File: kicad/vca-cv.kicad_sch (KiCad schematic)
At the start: 9 parts, among them Q14 2N3906, U19 TL072

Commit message: component positioning mostly done
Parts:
- C57, C58, C59: footprint rumblesan-standard-parts:C_Rect_L7.0mm_W3.5mm_P5.00mm -> rumblesan-standard-parts:C_Rect_L7.0mm_W2.5mm_P5.00mm
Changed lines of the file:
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@@
     (property "Reference" "C57" (id 0) (at 133.35 77.9612 90))
     (property "Value" "220pF" (id 1) (at 133.35 80.4981 90))
-    (property "Footprint" "rumblesan-standard-parts:C_Rect_L7.0mm_W3.5mm_P5.00mm" (id 2) (at 132.08 78.105 0)
+    (property "Footprint" "rumblesan-standard-parts:C_Rect_L7.0mm_W2.5mm_P5.00mm" (id 2) (at 132.08 78.105 0)
       (effects (font (size 1.27 1.27)) hide)
     )
@@
       (effects (font (size 1.27 1.27)) (justify left))
     )
-    (property "Footprint" "rumblesan-standard-parts:C_Rect_L7.0mm_W3.5mm_P5.00mm" (id 2) (at 215.265 60.96 90)
+    (property "Footprint" "rumblesan-standard-parts:C_Rect_L7.0mm_W2.5mm_P5.00mm" (id 2) (at 215.265 60.96 90)
       (effects (font (size 1.27 1.27)) hide)
     )
@@
       (effects (font (size 1.27 1.27)) (justify left))
     )
-    (property "Footprint" "rumblesan-standard-parts:C_Rect_L7.0mm_W3.5mm_P5.00mm" (id 2) (at 215.265 73.66 90)
-      (effects (font (size 1.27 1.27)) hide)
-    )
+    (property "Footprint" "rumblesan-standard-parts:C_Rect_L7.0mm_W2.5mm_P5.00mm" (id 2) (at 215.265 73.66 90)
+      (effects (font (size 1.27 1.27)) hide)
+    )

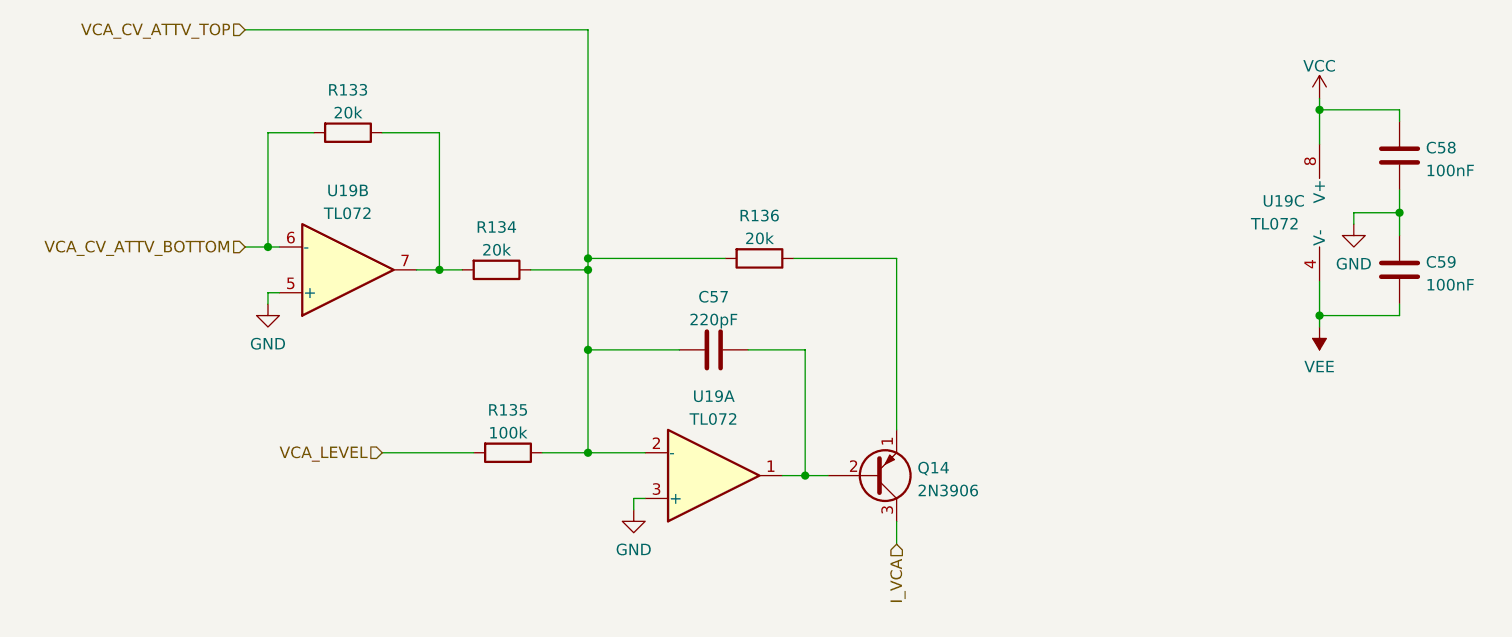
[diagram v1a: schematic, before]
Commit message: Full rejig to use attiny for divider
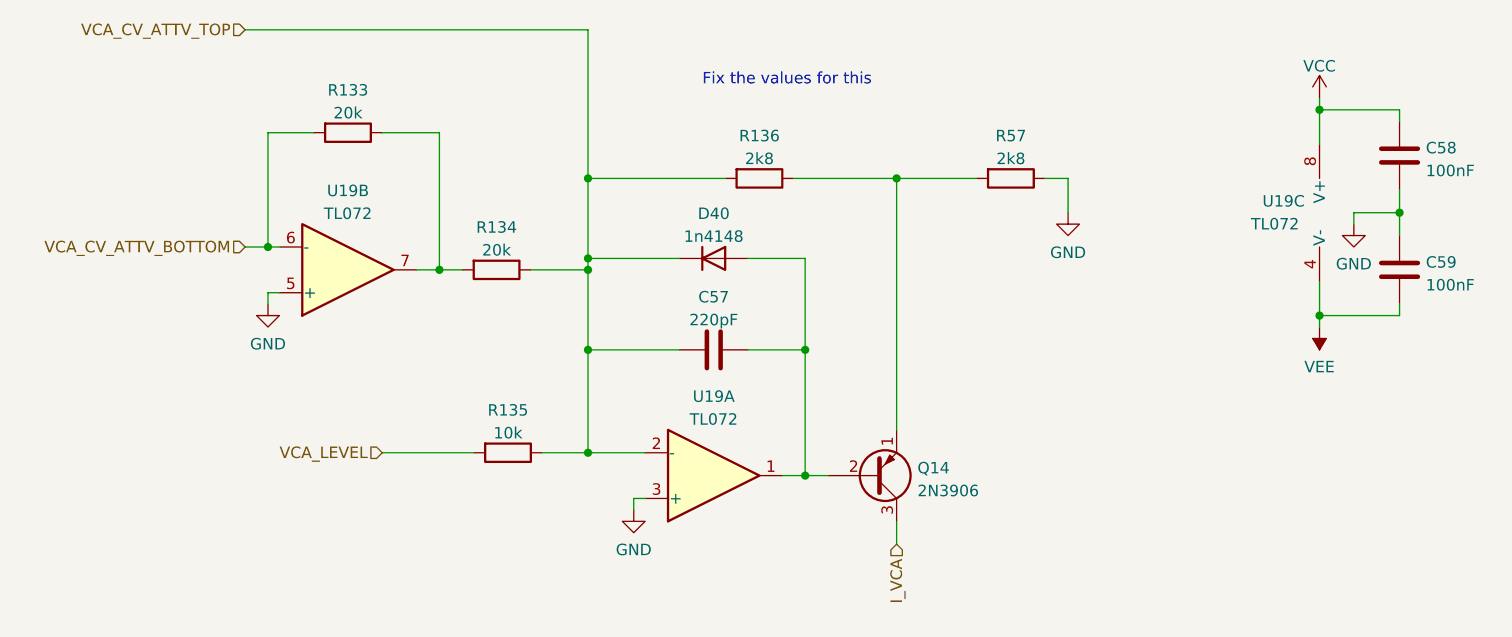
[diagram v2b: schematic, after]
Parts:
- added D40: 1n4148, rumblesan-standard-parts:D_DO-35_SOD27_P7.62mm_Horizontal, symbol Device:D
- added R57: 2k8, rumblesan-standard-parts:R_Axial_DIN0207_L6.3mm_D2.5mm_P10.16mm_Horizontal, symbol rumblesan-standard-parts:R
- C58, C59: Spec ceramic C0G -> ceramic X7R
- R135: value 100k -> 10k
- R136: value 20k -> 2k8
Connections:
- net GND: now also R57.1
- net VCA_CV_ATTV_TOP: now also D40.1 (K)
- net at C57.2, Q14.2 (B), U19.1: now also D40.2 (A)
- net at Q14.1 (E), R136.1: now also R57.2
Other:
- note added: "Fix the values for this"
- moved on the sheet: R136
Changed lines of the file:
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@@
     (comment 4 "Author: Guy John")
   )
+  (junction (at 143.51 83.82) (diameter 0) (color 0 0 0 0)
+  )
+  (junction (at 143.51 97.79) (diameter 0) (color 0 0 0 0)
+  )
+  (junction (at 102.87 74.93) (diameter 0) (color 0 0 0 0)
+  )
+  (junction (at 200.66 80.01) (diameter 0) (color 0 0 0 0)
+  )
+  (junction (at 119.38 74.93) (diameter 0) (color 0 0 0 0)
+  )
+  (junction (at 153.67 64.77) (diameter 0) (color 0 0 0 0)
+  )
+  (junction (at 209.55 68.58) (diameter 0) (color 0 0 0 0)
+  )
   (junction (at 119.38 73.66) (diameter 0) (color 0 0 0 0)
   )
-  (junction (at 143.51 97.79) (diameter 0) (color 0 0 0 0)
-  )
-  (junction (at 102.87 74.93) (diameter 0) (color 0 0 0 0)
-  )
-  (junction (at 200.66 80.01) (diameter 0) (color 0 0 0 0)
-  )
-  (junction (at 119.38 74.93) (diameter 0) (color 0 0 0 0)
-  )
-  (junction (at 209.55 68.58) (diameter 0) (color 0 0 0 0)
+  (junction (at 119.38 64.77) (diameter 0) (color 0 0 0 0)
   )
   (junction (at 83.82 72.39) (diameter 0) (color 0 0 0 0)
@@
   (junction (at 200.66 57.15) (diameter 0) (color 0 0 0 0)
   )
-  (wire (pts (xy 119.38 74.93) (xy 119.38 73.66))
-    (stroke (width 0) (type default) (color 0 0 0 0))
-  )
   (wire (pts (xy 153.67 102.87) (xy 153.67 105.41))
     (stroke (width 0) (type default) (color 0 0 0 0))
   )
+  (wire (pts (xy 170.18 64.77) (xy 172.72 64.77))
+    (stroke (width 0) (type default) (color 0 0 0 0))
+  )
   (wire (pts (xy 102.87 74.93) (xy 105.41 74.93))
     (stroke (width 0) (type default) (color 0 0 0 0))
@@
     (stroke (width 0) (type default) (color 0 0 0 0))
   )
-  (wire (pts (xy 153.67 73.66) (xy 153.67 92.71))
+  (wire (pts (xy 153.67 64.77) (xy 153.67 92.71))
+    (stroke (width 0) (type default) (color 0 0 0 0))
+  )
+  (wire (pts (xy 119.38 64.77) (xy 119.38 73.66))
+    (stroke (width 0) (type default) (color 0 0 0 0))
+  )
+  (wire (pts (xy 119.38 73.66) (xy 119.38 74.93))
     (stroke (width 0) (type default) (color 0 0 0 0))
   )
@@
     (stroke (width 0) (type default) (color 0 0 0 0))
   )
-  (wire (pts (xy 119.38 73.66) (xy 134.62 73.66))
+  (wire (pts (xy 119.38 64.77) (xy 134.62 64.77))
     (stroke (width 0) (type default) (color 0 0 0 0))
   )
@@
     (stroke (width 0) (type default) (color 0 0 0 0))
   )
-  (wire (pts (xy 142.24 73.66) (xy 153.67 73.66))
+  (wire (pts (xy 142.24 64.77) (xy 153.67 64.77))
     (stroke (width 0) (type default) (color 0 0 0 0))
   )
@@
     (stroke (width 0) (type default) (color 0 0 0 0))
   )
-  (wire (pts (xy 119.38 48.26) (xy 119.38 73.66))
+  (wire (pts (xy 153.67 64.77) (xy 162.56 64.77))
+    (stroke (width 0) (type default) (color 0 0 0 0))
+  )
+  (wire (pts (xy 119.38 73.66) (xy 129.54 73.66))
+    (stroke (width 0) (type default) (color 0 0 0 0))
+  )
+  (wire (pts (xy 119.38 48.26) (xy 119.38 64.77))
     (stroke (width 0) (type default) (color 0 0 0 0))
   )
@@
     (stroke (width 0) (type default) (color 0 0 0 0))
   )
+  (wire (pts (xy 137.16 73.66) (xy 143.51 73.66))
+    (stroke (width 0) (type default) (color 0 0 0 0))
+  )
   (wire (pts (xy 204.47 68.58) (xy 209.55 68.58))
     (stroke (width 0) (type default) (color 0 0 0 0))
@@
     (stroke (width 0) (type default) (color 0 0 0 0))
   )
+  (wire (pts (xy 172.72 64.77) (xy 172.72 68.58))
+    (stroke (width 0) (type default) (color 0 0 0 0))
+  )
   (wire (pts (xy 113.03 74.93) (xy 119.38 74.93))
     (stroke (width 0) (type default) (color 0 0 0 0))
@@
     (stroke (width 0) (type default) (color 0 0 0 0))
   )
+  (wire (pts (xy 143.51 73.66) (xy 143.51 83.82))
+    (stroke (width 0) (type default) (color 0 0 0 0))
+  )
   (wire (pts (xy 200.66 55.88) (xy 200.66 57.15))
     (stroke (width 0) (type default) (color 0 0 0 0))
@@
   (wire (pts (xy 85.09 77.47) (xy 83.82 77.47))
     (stroke (width 0) (type default) (color 0 0 0 0))
+  )
+  (text "Fix the values for this" (at 132.08 54.61 0)
+    (effects (font (size 1.27 1.27)) (justify left bottom))
   )
   (hierarchical_label "VCA_LEVEL" (shape input) (at 96.52 95.25 180)
@@
     (pin "1")
     (pin "2")
+  )
+  (symbol (lib_id "power:GND") (at 172.72 68.58 0) (unit 1)
+    (in_bom yes) (on_board yes) (fields_autoplaced)
+    (property "Reference" "#PWR0116" (id 0) (at 172.72 74.93 0)
+      (effects (font (size 1.27 1.27)) hide)
+    )
+    (property "Value" "GND" (id 1) (at 172.72 73.0234 0))
+    (property "Footprint" "" (id 2) (at 172.72 68.58 0)
+      (effects (font (size 1.27 1.27)) hide)
+    )
+    (property "Datasheet" "" (id 3) (at 172.72 68.58 0)
+      (effects (font (size 1.27 1.27)) hide)
+    )
+    (pin "1")
   )
   (symbol (lib_id "Amplifier_Operational:TL072") (at 133.35 97.79 0) (mirror x) (unit 1)
@@
     (pin "1")
   )
-  (symbol (lib_id "rumblesan-standard-parts:R") (at 138.43 73.66 90) (unit 1)
-    (in_bom yes) (on_board yes) (fields_autoplaced)
-    (property "Reference" "R136" (id 0) (at 138.43 68.9442 90))
-    (property "Value" "20k" (id 1) (at 138.43 71.4811 90))
-    (property "Footprint" "rumblesan-standard-parts:R_Axial_DIN0207_L6.3mm_D2.5mm_P10.16mm_Horizontal" (id 2) (at 140.97 71.12 90)
-      (effects (font (size 1.27 1.27)) hide)
-    )
-    (property "Datasheet" "~" (id 3) (at 138.43 67.31 0)
-      (effects (font (size 1.27 1.27)) hide)
-    )
-    (property "Tolerance" "1%" (id 4) (at 144.78 68.58 0)
-      (effects (font (size 1.27 1.27)) hide)
-    )
-    (property "Power" "0.5W" (id 5) (at 130.81 68.58 90)
-      (effects (font (size 1.27 1.27)) hide)
-    )
-    (property "Spec" "metal film" (id 6) (at 138.43 68.58 90)
+  (symbol (lib_id "rumblesan-standard-parts:R") (at 138.43 64.77 90) (unit 1)
+    (in_bom yes) (on_board yes) (fields_autoplaced)
+    (property "Reference" "R136" (id 0) (at 138.43 60.0542 90))
+    (property "Value" "2k8" (id 1) (at 138.43 62.5911 90))
+    (property "Footprint" "rumblesan-standard-parts:R_Axial_DIN0207_L6.3mm_D2.5mm_P10.16mm_Horizontal" (id 2) (at 140.97 62.23 90)
+      (effects (font (size 1.27 1.27)) hide)
+    )
+    (property "Datasheet" "~" (id 3) (at 138.43 58.42 0)
+      (effects (font (size 1.27 1.27)) hide)
+    )
+    (property "Tolerance" "1%" (id 4) (at 144.78 59.69 0)
+      (effects (font (size 1.27 1.27)) hide)
+    )
+    (property "Power" "0.5W" (id 5) (at 130.81 59.69 90)
+      (effects (font (size 1.27 1.27)) hide)
+    )
+    (property "Spec" "metal film" (id 6) (at 138.43 59.69 90)
       (effects (font (size 1.27 1.27)) hide)
     )
@@
     )
     (pin "1")
+  )
+  (symbol (lib_id "rumblesan-standard-parts:R") (at 166.37 64.77 90) (unit 1)
+    (in_bom yes) (on_board yes) (fields_autoplaced)
+    (property "Reference" "R57" (id 0) (at 166.37 60.0542 90))
+    (property "Value" "2k8" (id 1) (at 166.37 62.5911 90))
+    (property "Footprint" "rumblesan-standard-parts:R_Axial_DIN0207_L6.3mm_D2.5mm_P10.16mm_Horizontal" (id 2) (at 168.91 62.23 90)
+      (effects (font (size 1.27 1.27)) hide)
+    )
+    (property "Datasheet" "~" (id 3) (at 166.37 58.42 0)
+      (effects (font (size 1.27 1.27)) hide)
+    )
+    (property "Tolerance" "1%" (id 4) (at 172.72 59.69 0)
+      (effects (font (size 1.27 1.27)) hide)
+    )
+    (property "Power" "0.5W" (id 5) (at 158.75 59.69 90)
+      (effects (font (size 1.27 1.27)) hide)
+    )
+    (property "Spec" "metal film" (id 6) (at 166.37 59.69 90)
+      (effects (font (size 1.27 1.27)) hide)
+    )
+    (pin "1")
+    (pin "2")
   )
   (symbol (lib_id "rumblesan-standard-parts:R") (at 109.22 74.93 90) (unit 1)
@@
     )
     (property "Spec" "metal film" (id 6) (at 109.22 69.85 90)
+      (effects (font (size 1.27 1.27)) hide)
+    )
+    (pin "1")
+    (pin "2")
+  )
+  (symbol (lib_id "Device:D") (at 133.35 73.66 0) (unit 1)
+    (in_bom yes) (on_board yes) (fields_autoplaced)
+    (property "Reference" "D40" (id 0) (at 133.35 68.6902 0))
+    (property "Value" "1n4148" (id 1) (at 133.35 71.2271 0))
+    (property "Footprint" "rumblesan-standard-parts:D_DO-35_SOD27_P7.62mm_Horizontal" (id 2) (at 133.35 73.66 0)
+      (effects (font (size 1.27 1.27)) hide)
+    )
+    (property "Datasheet" "~" (id 3) (at 133.35 73.66 0)
       (effects (font (size 1.27 1.27)) hide)
     )
@@
     (in_bom yes) (on_board yes) (fields_autoplaced)
     (property "Reference" "R135" (id 0) (at 110.49 90.5342 90))
-    (property "Value" "100k" (id 1) (at 110.49 93.0711 90))
+    (property "Value" "10k" (id 1) (at 110.49 93.0711 90))
     (property "Footprint" "rumblesan-standard-parts:R_Axial_DIN0207_L6.3mm_D2.5mm_P10.16mm_Horizontal" (id 2) (at 113.03 92.71 90)
       (effects (font (size 1.27 1.27)) hide)
@@
       (effects (font (size 1.27 1.27)) hide)
     )
-    (property "Spec" "ceramic C0G" (id 4) (at 213.36 62.23 90)
+    (property "Spec" "ceramic X7R" (id 4) (at 213.36 62.23 90)
       (effects (font (size 1.27 1.27)) hide)
     )
@@
       (effects (font (size 1.27 1.27)) hide)
     )
-    (property "Spec" "ceramic C0G" (id 4) (at 213.36 74.93 90)
-      (effects (font (size 1.27 1.27)) hide)
-    )
+    (property "Spec" "ceramic X7R" (id 4) (at 213.36 74.93 90)
+      (effects (font (size 1.27 1.27)) hide)
+    )

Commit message: Tweaking VCA circuit
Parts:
- R133, R134: value 20k -> 100k
- R135: value 10k -> 330k
- R136: value 2k8 -> 33k
- R57: value 2k8 -> 1k
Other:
- note removed: "Fix the values for this"
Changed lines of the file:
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@@
     (stroke (width 0) (type default) (color 0 0 0 0))
-  )
-  (text "Fix the values for this" (at 132.08 54.61 0)
-    (effects (font (size 1.27 1.27)) (justify left bottom))
   )
   (hierarchical_label "VCA_LEVEL" (shape input) (at 96.52 95.25 180)
@@
     (in_bom yes) (on_board yes) (fields_autoplaced)
     (property "Reference" "R136" (id 0) (at 138.43 60.0542 90))
-    (property "Value" "2k8" (id 1) (at 138.43 62.5911 90))
+    (property "Value" "33k" (id 1) (at 138.43 62.5911 90))
     (property "Footprint" "rumblesan-standard-parts:R_Axial_DIN0207_L6.3mm_D2.5mm_P10.16mm_Horizontal" (id 2) (at 140.97 62.23 90)
       (effects (font (size 1.27 1.27)) hide)
@@
     (in_bom yes) (on_board yes) (fields_autoplaced)
     (property "Reference" "R57" (id 0) (at 166.37 60.0542 90))
-    (property "Value" "2k8" (id 1) (at 166.37 62.5911 90))
+    (property "Value" "1k" (id 1) (at 166.37 62.5911 90))
     (property "Footprint" "rumblesan-standard-parts:R_Axial_DIN0207_L6.3mm_D2.5mm_P10.16mm_Horizontal" (id 2) (at 168.91 62.23 90)
       (effects (font (size 1.27 1.27)) hide)
@@
     (in_bom yes) (on_board yes) (fields_autoplaced)
     (property "Reference" "R134" (id 0) (at 109.22 70.2142 90))
-    (property "Value" "20k" (id 1) (at 109.22 72.7511 90))
+    (property "Value" "100k" (id 1) (at 109.22 72.7511 90))
     (property "Footprint" "rumblesan-standard-parts:R_Axial_DIN0207_L6.3mm_D2.5mm_P10.16mm_Horizontal" (id 2) (at 111.76 72.39 90)
       (effects (font (size 1.27 1.27)) hide)
@@
     (in_bom yes) (on_board yes) (fields_autoplaced)
     (property "Reference" "R135" (id 0) (at 110.49 90.5342 90))
-    (property "Value" "10k" (id 1) (at 110.49 93.0711 90))
+    (property "Value" "330k" (id 1) (at 110.49 93.0711 90))
     (property "Footprint" "rumblesan-standard-parts:R_Axial_DIN0207_L6.3mm_D2.5mm_P10.16mm_Horizontal" (id 2) (at 113.03 92.71 90)
       (effects (font (size 1.27 1.27)) hide)
@@
     (in_bom yes) (on_board yes) (fields_autoplaced)
     (property "Reference" "R133" (id 0) (at 92.71 54.9742 90))
-    (property "Value" "20k" (id 1) (at 92.71 57.5111 90))
+    (property "Value" "100k" (id 1) (at 92.71 57.5111 90))
     (property "Footprint" "rumblesan-standard-parts:R_Axial_DIN0207_L6.3mm_D2.5mm_P10.16mm_Horizontal" (id 2) (at 95.25 57.15 90)
       (effects (font (size 1.27 1.27)) hide)

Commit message: Changing name to the mercurial machine
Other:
- title: (none) -> The Mercurial Machine
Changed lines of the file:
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@@
   (paper "A4")
   (title_block
+    (title "The Mercurial Machine")
+    (date "2023-05-13")
+    (rev "r02")
     (comment 2 "creativecommons.org/licenses/by/4.0/")
     (comment 3 "License: CC BY 4.0")
